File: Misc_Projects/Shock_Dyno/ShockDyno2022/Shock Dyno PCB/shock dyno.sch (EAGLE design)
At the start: 31 parts, among them IC1 ADS8332IBPWR, J1 1985195, K1 T9GS1L14-5, U1 REF5040AIDR

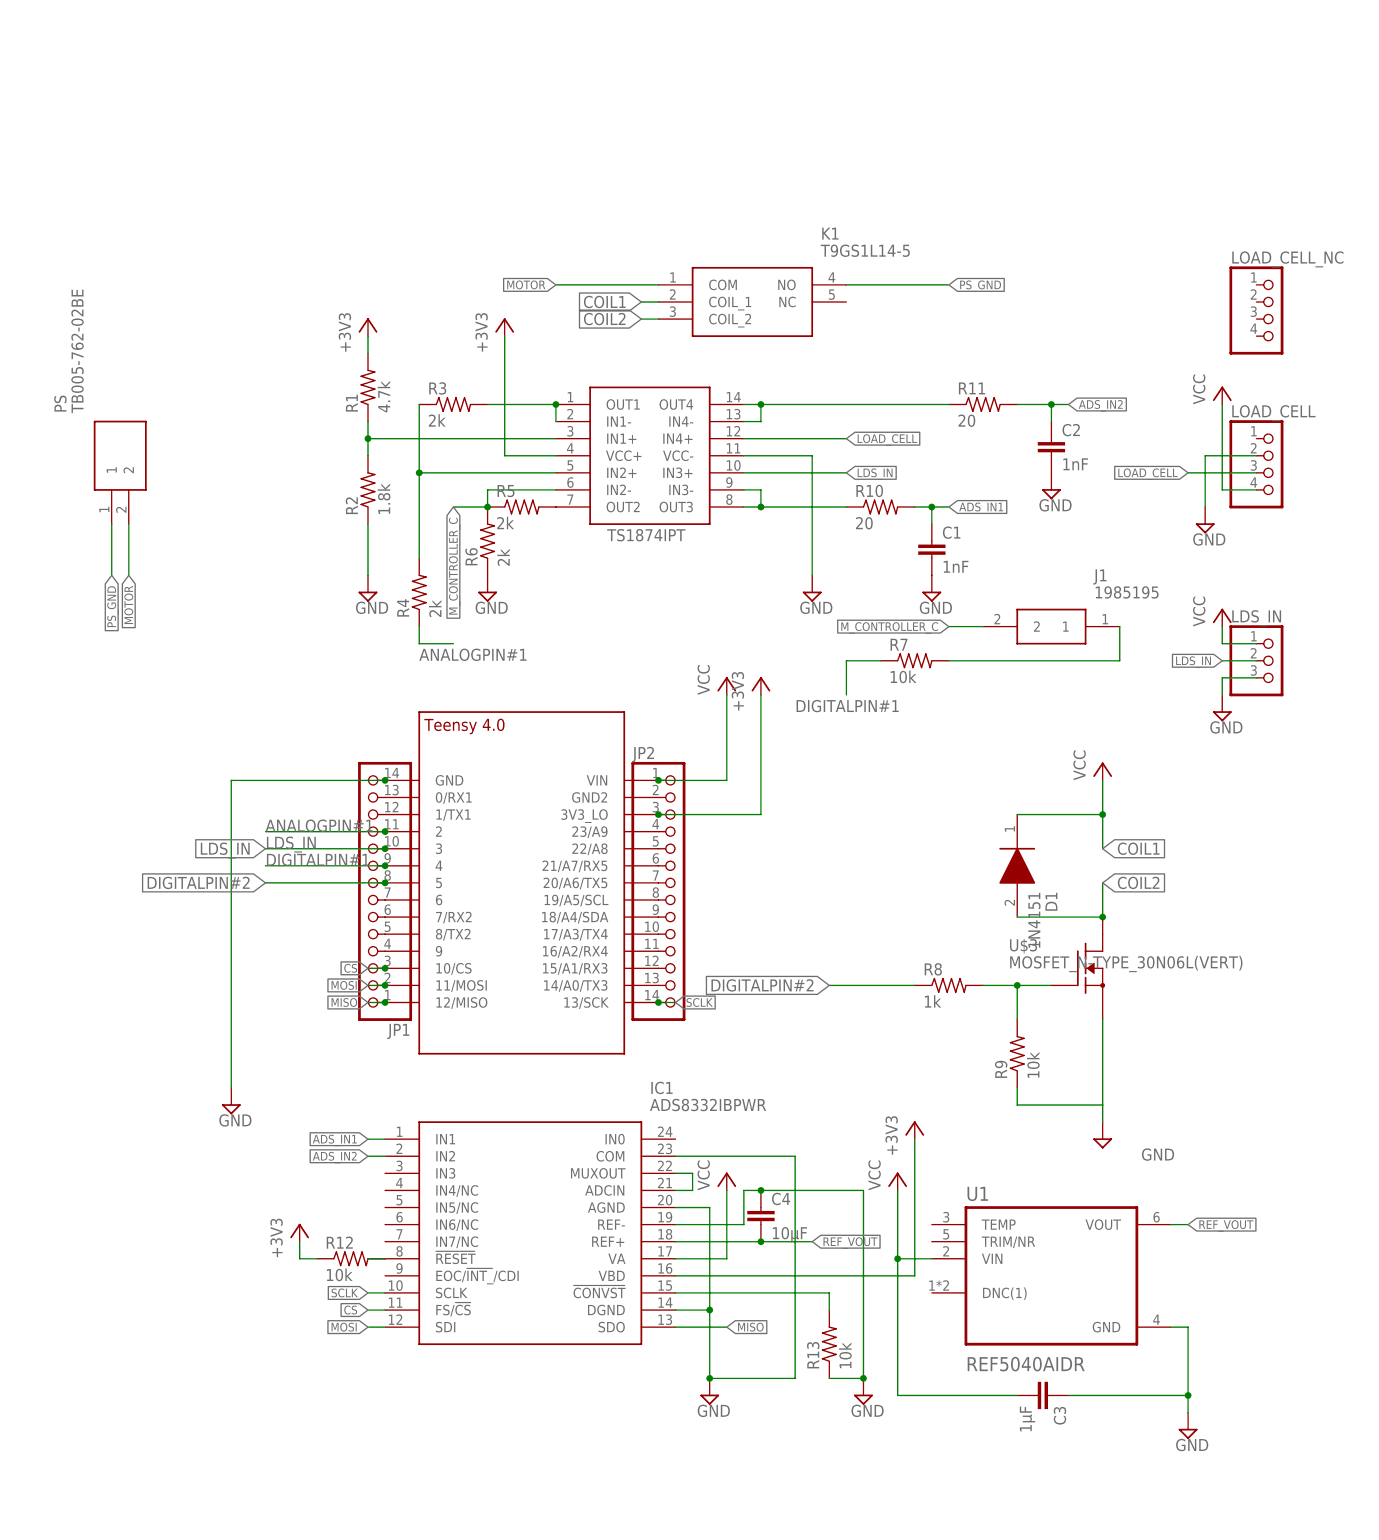
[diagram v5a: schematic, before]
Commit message: final touches to shock dyno PCB part 2
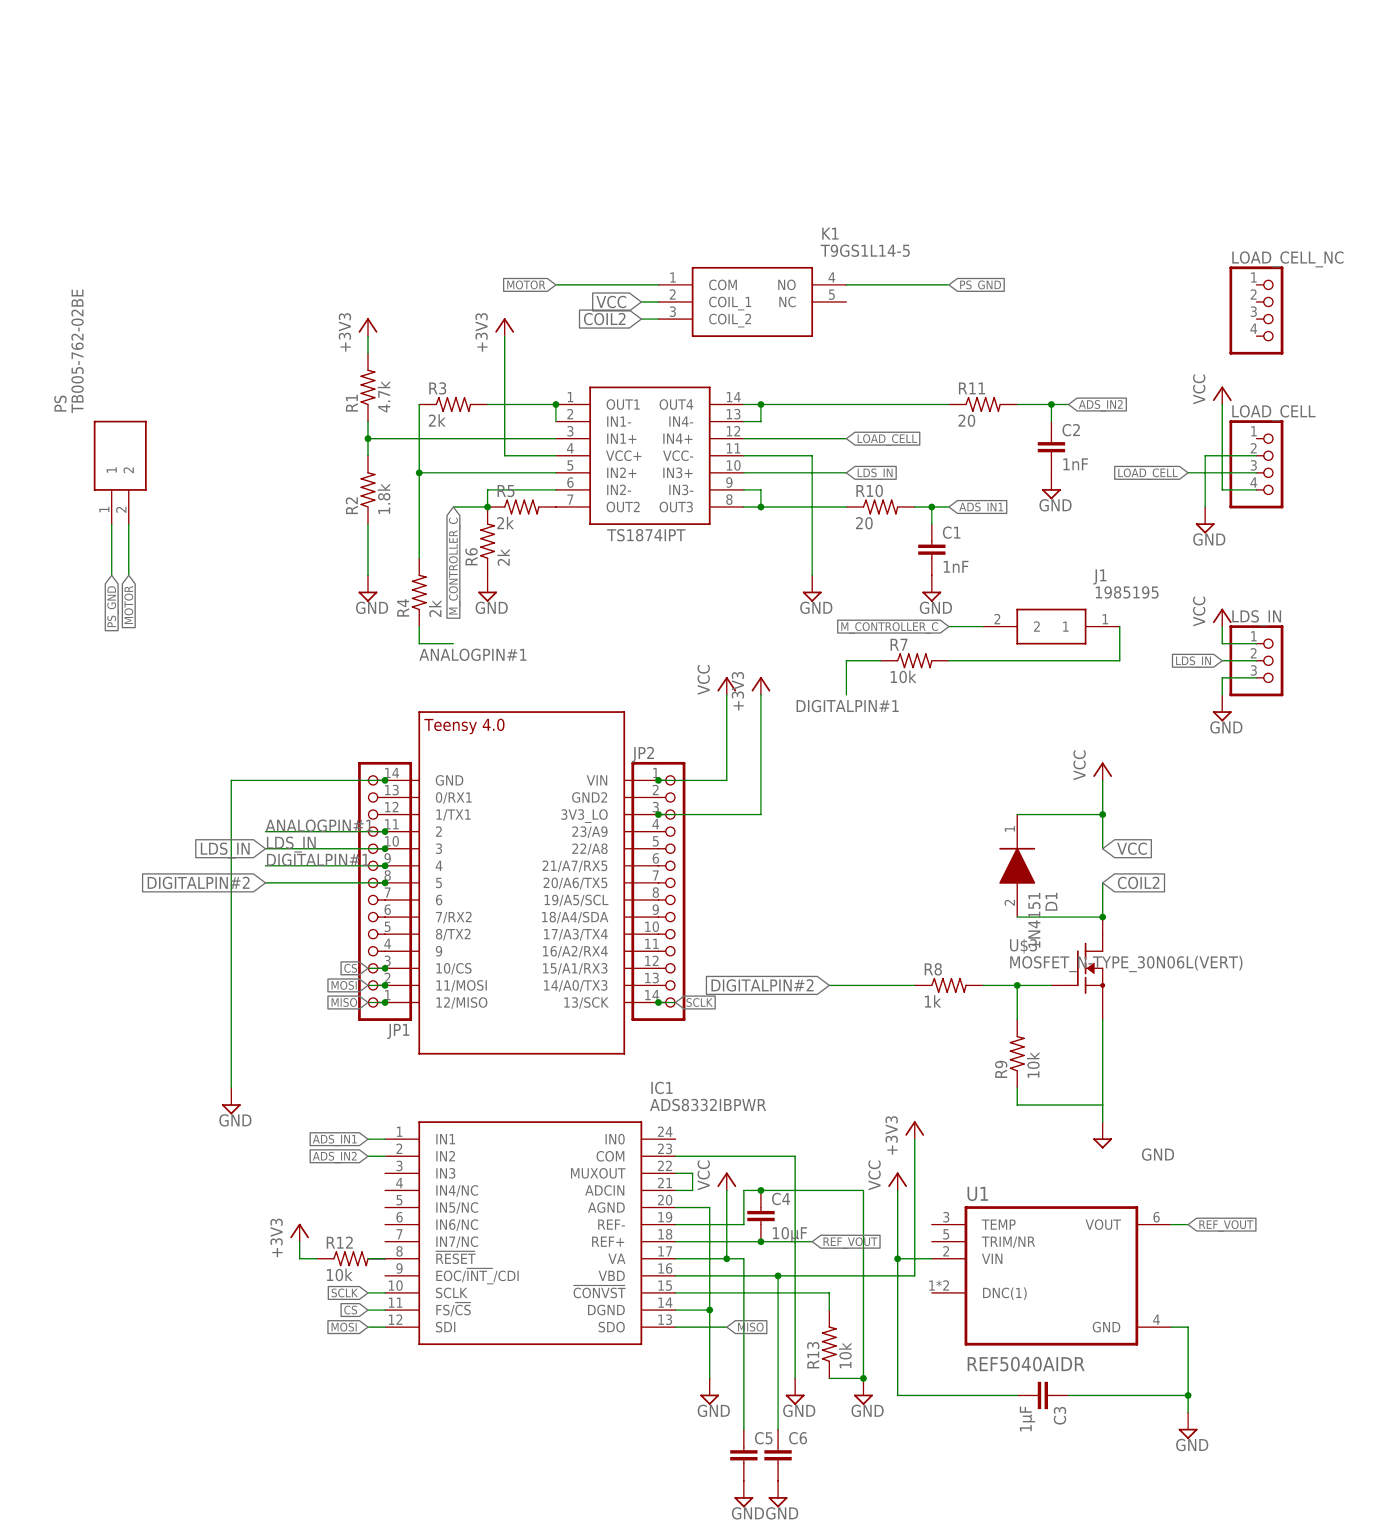
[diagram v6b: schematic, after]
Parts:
- added C5, C6: (no value), GTOR - Passive Components:CAP_SMDC0603
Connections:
- removed net COIL1: D1.K, K1.COIL_1
- net +3V3: now also C6.1
- net GND: now also C5.2, C6.2
- net VCC: now also C5.1, D1.K, K1.COIL_1
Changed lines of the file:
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@@
 <part name="JP2" library="GTOR - Connectors" deviceset="PINHD-1X14" device="" package3d_urn="urn:adsk.eagle:package:22417/2"/>
 <part name="R13" library="GTOR - Passive Components" deviceset="RES_SMD" device="R0603" package3d_urn="urn:adsk.eagle:package:23555/3" value="10k"/>
+<part name="C5" library="GTOR - Passive Components" deviceset="CAP_SMD" device="C0603" package3d_urn="urn:adsk.eagle:package:23616/2"/>
+<part name="C6" library="GTOR - Passive Components" deviceset="CAP_SMD" device="C0603" package3d_urn="urn:adsk.eagle:package:23616/2"/>
+<part name="SUPPLY5" library="GTOR - Documation Frame" deviceset="GND" device=""/>
+<part name="SUPPLY6" library="GTOR - Documation Frame" deviceset="GND" device=""/>
+<part name="SUPPLY7" library="GTOR - Documation Frame" deviceset="GND" device=""/>
 </parts>
 <sheets>
@@
 <attribute name="VALUE" x="66.802" y="-77.47" size="1.778" layer="96" rot="R90"/>
 </instance>
+<instance part="C5" gate="G$1" x="50.8" y="-88.9" smashed="yes">
+<attribute name="NAME" x="52.324" y="-88.519" size="1.778" layer="95"/>
+<attribute name="VALUE" x="52.324" y="-93.599" size="1.778" layer="96"/>
+</instance>
+<instance part="C6" gate="G$1" x="55.88" y="-88.9" smashed="yes">
+<attribute name="NAME" x="57.404" y="-88.519" size="1.778" layer="95"/>
+<attribute name="VALUE" x="57.404" y="-93.599" size="1.778" layer="96"/>
+</instance>
+<instance part="SUPPLY5" gate="GND" x="58.42" y="-81.28" smashed="yes">
+<attribute name="VALUE" x="56.515" y="-84.455" size="1.778" layer="96"/>
+</instance>
+<instance part="SUPPLY6" gate="GND" x="50.8" y="-96.52" smashed="yes">
+<attribute name="VALUE" x="48.895" y="-99.695" size="1.778" layer="96"/>
+</instance>
+<instance part="SUPPLY7" gate="GND" x="55.88" y="-96.52" smashed="yes">
+<attribute name="VALUE" x="53.975" y="-99.695" size="1.778" layer="96"/>
+</instance>
 </instances>
 <busses>
@@
 </segment>
 <segment>
+<pinref part="SUPPLY13" gate="GND" pin="GND"/>
 <pinref part="IC1" gate="G$1" pin="DGND"/>
+<wire x1="40.64" y1="-68.58" x2="45.72" y2="-68.58" width="0.1524" layer="91"/>
+<wire x1="45.72" y1="-68.58" x2="45.72" y2="-78.74" width="0.1524" layer="91"/>
+<junction x="45.72" y="-68.58"/>
 <pinref part="IC1" gate="G$1" pin="AGND"/>
 <wire x1="40.64" y1="-53.34" x2="45.72" y2="-53.34" width="0.1524" layer="91"/>
 <wire x1="45.72" y1="-53.34" x2="45.72" y2="-68.58" width="0.1524" layer="91"/>
-<wire x1="40.64" y1="-68.58" x2="45.72" y2="-68.58" width="0.1524" layer="91"/>
-<pinref part="SUPPLY13" gate="GND" pin="GND"/>
-<wire x1="45.72" y1="-68.58" x2="45.72" y2="-78.74" width="0.1524" layer="91"/>
-<junction x="45.72" y="-68.58"/>
-<pinref part="IC1" gate="G$1" pin="COM"/>
-<wire x1="40.64" y1="-45.72" x2="58.42" y2="-45.72" width="0.1524" layer="91"/>
-<wire x1="58.42" y1="-45.72" x2="58.42" y2="-78.74" width="0.1524" layer="91"/>
-<wire x1="58.42" y1="-78.74" x2="45.72" y2="-78.74" width="0.1524" layer="91"/>
-<junction x="45.72" y="-78.74"/>
 </segment>
 <segment>
@@
 <wire x1="121.92" y1="25.4" x2="121.92" y2="22.86" width="0.1524" layer="91"/>
 </segment>
+<segment>
+<pinref part="IC1" gate="G$1" pin="COM"/>
+<wire x1="40.64" y1="-45.72" x2="58.42" y2="-45.72" width="0.1524" layer="91"/>
+<wire x1="58.42" y1="-45.72" x2="58.42" y2="-78.74" width="0.1524" layer="91"/>
+<pinref part="SUPPLY5" gate="GND" pin="GND"/>
+</segment>
+<segment>
+<pinref part="C5" gate="G$1" pin="2"/>
+<pinref part="SUPPLY6" gate="GND" pin="GND"/>
+</segment>
+<segment>
+<pinref part="C6" gate="G$1" pin="2"/>
+<pinref part="SUPPLY7" gate="GND" pin="GND"/>
+</segment>
 </net>
 <net name="+3V3" class="0">
@@
 <segment>
 <pinref part="IC1" gate="G$1" pin="VBD"/>
-<wire x1="40.64" y1="-63.5" x2="76.2" y2="-63.5" width="0.1524" layer="91"/>
+<wire x1="40.64" y1="-63.5" x2="55.88" y2="-63.5" width="0.1524" layer="91"/>
+<wire x1="55.88" y1="-63.5" x2="76.2" y2="-63.5" width="0.1524" layer="91"/>
 <wire x1="76.2" y1="-63.5" x2="76.2" y2="-43.18" width="0.1524" layer="91"/>
 <pinref part="+3V4" gate="G$1" pin="+3V3"/>
+<wire x1="55.88" y1="-63.5" x2="55.88" y2="-86.36" width="0.1524" layer="91"/>
+<junction x="55.88" y="-63.5"/>
+<pinref part="C6" gate="G$1" pin="1"/>
 </segment>
 <segment>
@@
 <pinref part="JP1" gate="A" pin="9"/>
 <junction x="-2.54" y="-2.54"/>
-</segment>
-</net>
-<net name="COIL1" class="0">
-<segment>
-<pinref part="P+4" gate="VCC" pin="VCC"/>
-<wire x1="104.14" y1="10.16" x2="104.14" y2="5.08" width="0.1524" layer="91"/>
-<pinref part="D1" gate="G$1" pin="K"/>
-<wire x1="104.14" y1="5.08" x2="104.14" y2="0" width="0.1524" layer="91"/>
-<wire x1="91.44" y1="5.08" x2="104.14" y2="5.08" width="0.1524" layer="91"/>
-<junction x="104.14" y="5.08"/>
-<label x="104.14" y="0" size="1.778" layer="95" xref="yes"/>
-</segment>
-<segment>
-<pinref part="K1" gate="G$1" pin="COIL_1"/>
-<wire x1="38.1" y1="81.28" x2="35.56" y2="81.28" width="0.1524" layer="91"/>
-<label x="35.56" y="81.28" size="1.778" layer="95" rot="R180" xref="yes"/>
 </segment>
 </net>
@@
 <wire x1="48.26" y1="-60.96" x2="48.26" y2="-50.8" width="0.1524" layer="91"/>
 <pinref part="P+6" gate="VCC" pin="VCC"/>
+<wire x1="48.26" y1="-60.96" x2="50.8" y2="-60.96" width="0.1524" layer="91"/>
+<wire x1="50.8" y1="-60.96" x2="50.8" y2="-86.36" width="0.1524" layer="91"/>
+<junction x="48.26" y="-60.96"/>
+<pinref part="C5" gate="G$1" pin="1"/>
 </segment>
 <segment>
@@
 <junction x="38.1" y="10.16"/>
 </segment>
-</net>
+<segment>
+<pinref part="P+4" gate="VCC" pin="VCC"/>
+<wire x1="104.14" y1="10.16" x2="104.14" y2="5.08" width="0.1524" layer="91"/>
+<pinref part="D1" gate="G$1" pin="K"/>
+<wire x1="104.14" y1="5.08" x2="104.14" y2="0" width="0.1524" layer="91"/>
+<wire x1="91.44" y1="5.08" x2="104.14" y2="5.08" width="0.1524" layer="91"/>
+<junction x="104.14" y="5.08"/>
+<label x="104.14" y="0" size="1.778" layer="95" xref="yes"/>
+</segment>
+<segment>
+<pinref part="K1" gate="G$1" pin="COIL_1"/>
+<wire x1="38.1" y1="81.28" x2="35.56" y2="81.28" width="0.1524" layer="91"/>
+<label x="35.56" y="81.28" size="1.778" layer="95" rot="R180" xref="yes"/>
+</segment>
+</net>

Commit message: final touches to shock dyno PCB part 3
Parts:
- C5, C6: value (none) -> 0.1μF
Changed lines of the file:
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@@
 <part name="JP2" library="GTOR - Connectors" deviceset="PINHD-1X14" device="" package3d_urn="urn:adsk.eagle:package:22417/2"/>
 <part name="R13" library="GTOR - Passive Components" deviceset="RES_SMD" device="R0603" package3d_urn="urn:adsk.eagle:package:23555/3" value="10k"/>
-<part name="C5" library="GTOR - Passive Components" deviceset="CAP_SMD" device="C0603" package3d_urn="urn:adsk.eagle:package:23616/2"/>
-<part name="C6" library="GTOR - Passive Components" deviceset="CAP_SMD" device="C0603" package3d_urn="urn:adsk.eagle:package:23616/2"/>
+<part name="C5" library="GTOR - Passive Components" deviceset="CAP_SMD" device="C0603" package3d_urn="urn:adsk.eagle:package:23616/2" value="0.1μF"/>
+<part name="C6" library="GTOR - Passive Components" deviceset="CAP_SMD" device="C0603" package3d_urn="urn:adsk.eagle:package:23616/2" value="0.1μF"/>
 <part name="SUPPLY5" library="GTOR - Documation Frame" deviceset="GND" device=""/>
 <part name="SUPPLY6" library="GTOR - Documation Frame" deviceset="GND" device=""/>
@@
 <instance part="C5" gate="G$1" x="50.8" y="-88.9" smashed="yes">
 <attribute name="NAME" x="52.324" y="-88.519" size="1.778" layer="95"/>
-<attribute name="VALUE" x="52.324" y="-93.599" size="1.778" layer="96"/>
+<attribute name="VALUE" x="42.164" y="-93.599" size="1.778" layer="96"/>
 </instance>
 <instance part="C6" gate="G$1" x="55.88" y="-88.9" smashed="yes">

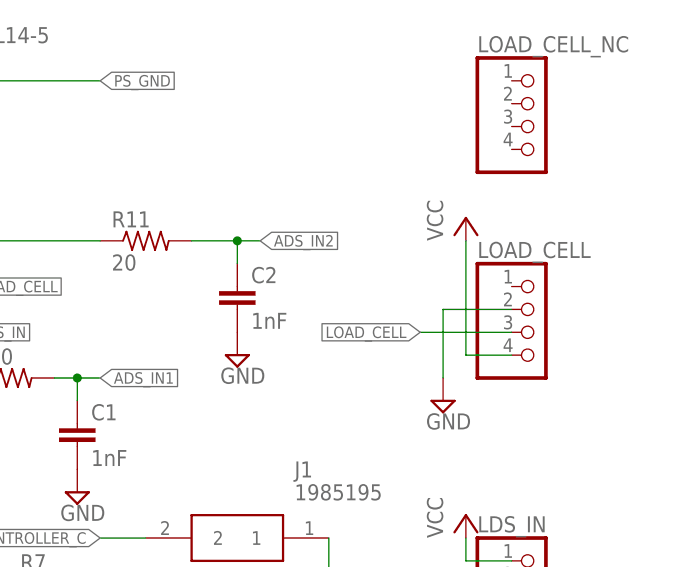
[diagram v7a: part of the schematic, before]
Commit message: oriented load cell connector correctly
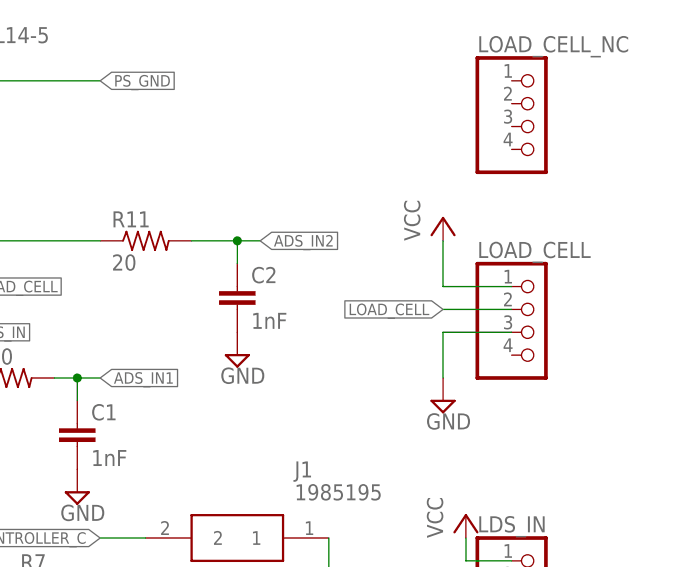
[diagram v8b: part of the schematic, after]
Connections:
- net GND: now also LOAD_CELL.3; no longer LOAD_CELL.2
- net LOAD_CELL: now also LOAD_CELL.2; no longer LOAD_CELL.3
- net VCC: now also LOAD_CELL.1; no longer LOAD_CELL.4
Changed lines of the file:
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@@
 <attribute name="VALUE" x="117.475" y="45.085" size="1.778" layer="96"/>
 </instance>
-<instance part="P+7" gate="VCC" x="121.92" y="68.58" smashed="yes">
-<attribute name="VALUE" x="119.38" y="66.04" size="1.778" layer="96" rot="R90"/>
+<instance part="P+7" gate="VCC" x="119.38" y="68.58" smashed="yes">
+<attribute name="VALUE" x="116.84" y="66.04" size="1.778" layer="96" rot="R90"/>
 </instance>
 <instance part="LDS_IN" gate="A" x="129.54" y="27.94" smashed="yes">
@@
 </segment>
 <segment>
-<pinref part="LOAD_CELL" gate="A" pin="2"/>
-<wire x1="127" y1="58.42" x2="119.38" y2="58.42" width="0.1524" layer="91"/>
-<pinref part="SUPPLY15" gate="GND" pin="GND"/>
-<wire x1="119.38" y1="58.42" x2="119.38" y2="50.8" width="0.1524" layer="91"/>
-</segment>
-<segment>
 <pinref part="LDS_IN" gate="A" pin="3"/>
 <wire x1="127" y1="25.4" x2="121.92" y2="25.4" width="0.1524" layer="91"/>
@@
 <pinref part="C6" gate="G$1" pin="2"/>
 <pinref part="SUPPLY7" gate="GND" pin="GND"/>
+</segment>
+<segment>
+<pinref part="SUPPLY15" gate="GND" pin="GND"/>
+<wire x1="119.38" y1="50.8" x2="119.38" y2="55.88" width="0.1524" layer="91"/>
+<pinref part="LOAD_CELL" gate="A" pin="3"/>
+<wire x1="119.38" y1="55.88" x2="127" y2="55.88" width="0.1524" layer="91"/>
 </segment>
 </net>
@@
 </segment>
 <segment>
-<pinref part="LOAD_CELL" gate="A" pin="3"/>
-<wire x1="127" y1="55.88" x2="116.84" y2="55.88" width="0.1524" layer="91"/>
-<label x="116.84" y="55.88" size="1.27" layer="95" rot="R180" xref="yes"/>
+<pinref part="LOAD_CELL" gate="A" pin="2"/>
+<wire x1="127" y1="58.42" x2="119.38" y2="58.42" width="0.1524" layer="91"/>
+<label x="119.38" y="58.42" size="1.27" layer="95" rot="R180" xref="yes"/>
 </segment>
 </net>
@@
 </segment>
 <segment>
-<pinref part="LOAD_CELL" gate="A" pin="4"/>
-<wire x1="127" y1="53.34" x2="121.92" y2="53.34" width="0.1524" layer="91"/>
-<wire x1="121.92" y1="53.34" x2="121.92" y2="66.04" width="0.1524" layer="91"/>
-<pinref part="P+7" gate="VCC" pin="VCC"/>
-</segment>
-<segment>
 <pinref part="LDS_IN" gate="A" pin="1"/>
 <wire x1="127" y1="30.48" x2="121.92" y2="30.48" width="0.1524" layer="91"/>
@@
 <label x="35.56" y="81.28" size="1.778" layer="95" rot="R180" xref="yes"/>
 </segment>
-</net>
+<segment>
+<pinref part="P+7" gate="VCC" pin="VCC"/>
+<wire x1="119.38" y1="66.04" x2="119.38" y2="60.96" width="0.1524" layer="91"/>
+<pinref part="LOAD_CELL" gate="A" pin="1"/>
+<wire x1="119.38" y1="60.96" x2="127" y2="60.96" width="0.1524" layer="91"/>
+</segment>
+</net>
